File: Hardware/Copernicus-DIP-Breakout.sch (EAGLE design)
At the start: 12 parts, among them U1 COPERNICUS

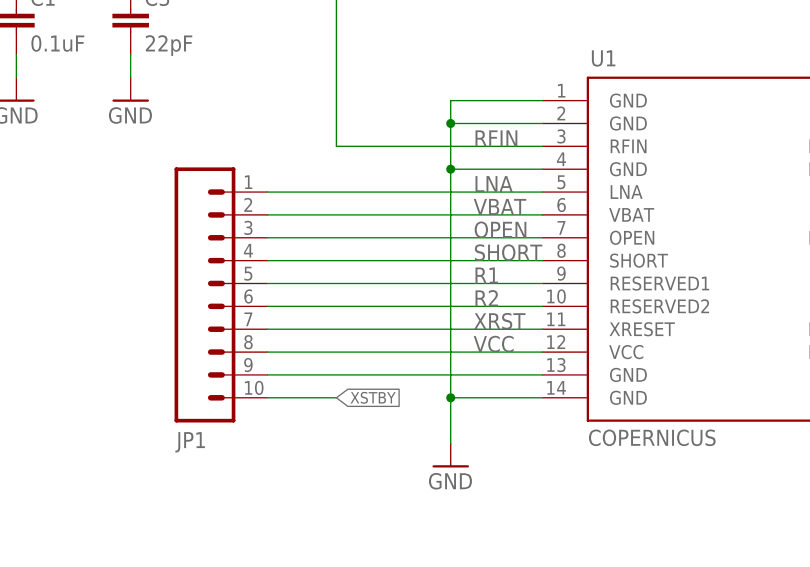
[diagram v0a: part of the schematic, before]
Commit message: Fix silk screen on board file
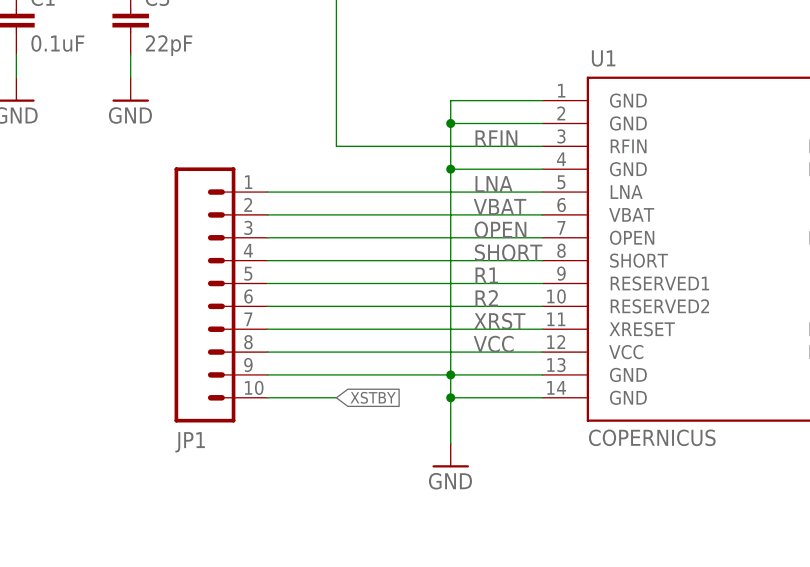
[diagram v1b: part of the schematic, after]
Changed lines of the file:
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@@
 <grid distance="0.1" unitdist="inch" unit="inch" style="lines" multiple="1" display="no" altdistance="0.01" altunitdist="inch" altunit="inch"/>
 <layers>
-<layer number="1" name="Top" color="4" fill="1" visible="yes" active="no"/>
-<layer number="2" name="Route2" color="1" fill="3" visible="yes" active="no"/>
-<layer number="3" name="Route3" color="4" fill="3" visible="yes" active="no"/>
-<layer number="4" name="Route4" color="1" fill="4" visible="yes" active="no"/>
-<layer number="5" name="Route5" color="4" fill="4" visible="yes" active="no"/>
-<layer number="6" name="Route6" color="1" fill="8" visible="yes" active="no"/>
-<layer number="7" name="Route7" color="4" fill="8" visible="yes" active="no"/>
-<layer number="8" name="Route8" color="1" fill="2" visible="yes" active="no"/>
-<layer number="9" name="Route9" color="4" fill="2" visible="yes" active="no"/>
-<layer number="10" name="Route10" color="1" fill="7" visible="yes" active="no"/>
-<layer number="11" name="Route11" color="4" fill="7" visible="yes" active="no"/>
-<layer number="12" name="Route12" color="1" fill="5" visible="yes" active="no"/>
-<layer number="13" name="Route13" color="4" fill="5" visible="yes" active="no"/>
-<layer number="14" name="Route14" color="1" fill="6" visible="yes" active="no"/>
-<layer number="15" name="Route15" color="4" fill="6" visible="yes" active="no"/>
-<layer number="16" name="Bottom" color="1" fill="1" visible="yes" active="no"/>
-<layer number="17" name="Pads" color="2" fill="1" visible="yes" active="no"/>
-<layer number="18" name="Vias" color="2" fill="1" visible="yes" active="no"/>
-<layer number="19" name="Unrouted" color="6" fill="1" visible="yes" active="no"/>
-<layer number="20" name="Dimension" color="15" fill="1" visible="yes" active="no"/>
-<layer number="21" name="tPlace" color="16" fill="1" visible="yes" active="no"/>
-<layer number="22" name="bPlace" color="14" fill="1" visible="yes" active="no"/>
-<layer number="23" name="tOrigins" color="15" fill="1" visible="yes" active="no"/>
-<layer number="24" name="bOrigins" color="15" fill="1" visible="yes" active="no"/>
-<layer number="25" name="tNames" color="7" fill="1" visible="yes" active="no"/>
-<layer number="26" name="bNames" color="7" fill="1" visible="yes" active="no"/>
-<layer number="27" name="tValues" color="7" fill="1" visible="yes" active="no"/>
-<layer number="28" name="bValues" color="7" fill="1" visible="yes" active="no"/>
+<layer number="1" name="Top" color="4" fill="1" visible="no" active="no"/>
+<layer number="2" name="Route2" color="1" fill="3" visible="no" active="no"/>
+<layer number="3" name="Route3" color="4" fill="3" visible="no" active="no"/>
+<layer number="4" name="Route4" color="1" fill="4" visible="no" active="no"/>
+<layer number="5" name="Route5" color="4" fill="4" visible="no" active="no"/>
+<layer number="6" name="Route6" color="1" fill="8" visible="no" active="no"/>
+<layer number="7" name="Route7" color="4" fill="8" visible="no" active="no"/>
+<layer number="8" name="Route8" color="1" fill="2" visible="no" active="no"/>
+<layer number="9" name="Route9" color="4" fill="2" visible="no" active="no"/>
+<layer number="10" name="Route10" color="1" fill="7" visible="no" active="no"/>
+<layer number="11" name="Route11" color="4" fill="7" visible="no" active="no"/>
+<layer number="12" name="Route12" color="1" fill="5" visible="no" active="no"/>
+<layer number="13" name="Route13" color="4" fill="5" visible="no" active="no"/>
+<layer number="14" name="Route14" color="1" fill="6" visible="no" active="no"/>
+<layer number="15" name="Route15" color="4" fill="6" visible="no" active="no"/>
+<layer number="16" name="Bottom" color="1" fill="1" visible="no" active="no"/>
+<layer number="17" name="Pads" color="2" fill="1" visible="no" active="no"/>
+<layer number="18" name="Vias" color="2" fill="1" visible="no" active="no"/>
+<layer number="19" name="Unrouted" color="6" fill="1" visible="no" active="no"/>
+<layer number="20" name="Dimension" color="15" fill="1" visible="no" active="no"/>
+<layer number="21" name="tPlace" color="16" fill="1" visible="no" active="no"/>
+<layer number="22" name="bPlace" color="14" fill="1" visible="no" active="no"/>
+<layer number="23" name="tOrigins" color="15" fill="1" visible="no" active="no"/>
+<layer number="24" name="bOrigins" color="15" fill="1" visible="no" active="no"/>
+<layer number="25" name="tNames" color="7" fill="1" visible="no" active="no"/>
+<layer number="26" name="bNames" color="7" fill="1" visible="no" active="no"/>
+<layer number="27" name="tValues" color="7" fill="1" visible="no" active="no"/>
+<layer number="28" name="bValues" color="7" fill="1" visible="no" active="no"/>
 <layer number="29" name="tStop" color="7" fill="3" visible="no" active="no"/>
 <layer number="30" name="bStop" color="7" fill="6" visible="no" active="no"/>
@@
 <layer number="35" name="tGlue" color="7" fill="4" visible="no" active="no"/>
 <layer number="36" name="bGlue" color="7" fill="5" visible="no" active="no"/>
-<layer number="37" name="tTest" color="7" fill="1" visible="yes" active="no"/>
-<layer number="38" name="bTest" color="7" fill="1" visible="yes" active="no"/>
+<layer number="37" name="tTest" color="7" fill="1" visible="no" active="no"/>
+<layer number="38" name="bTest" color="7" fill="1" visible="no" active="no"/>
 <layer number="39" name="tKeepout" color="4" fill="11" visible="no" active="no"/>
 <layer number="40" name="bKeepout" color="1" fill="11" visible="no" active="no"/>
@@
 <layer number="44" name="Drills" color="7" fill="1" visible="no" active="no"/>
 <layer number="45" name="Holes" color="7" fill="1" visible="no" active="no"/>
-<layer number="46" name="Milling" color="3" fill="1" visible="yes" active="no"/>
-<layer number="47" name="Measures" color="7" fill="1" visible="yes" active="no"/>
-<layer number="48" name="Document" color="7" fill="1" visible="yes" active="no"/>
-<layer number="49" name="Reference" color="7" fill="1" visible="yes" active="no"/>
-<layer number="50" name="dxf" color="7" fill="1" visible="yes" active="no"/>
-<layer number="51" name="tDocu" color="6" fill="1" visible="yes" active="no"/>
-<layer number="52" name="bDocu" color="7" fill="1" visible="yes" active="no"/>
-<layer number="53" name="tGND_GNDA" color="7" fill="9" visible="yes" active="no"/>
-<layer number="54" name="bGND_GNDA" color="1" fill="9" visible="yes" active="no"/>
-<layer number="56" name="wert" color="7" fill="1" visible="yes" active="no"/>
+<layer number="46" name="Milling" color="3" fill="1" visible="no" active="no"/>
+<layer number="47" name="Measures" color="7" fill="1" visible="no" active="no"/>
+<layer number="48" name="Document" color="7" fill="1" visible="no" active="no"/>
+<layer number="49" name="Reference" color="7" fill="1" visible="no" active="no"/>
+<layer number="50" name="dxf" color="7" fill="1" visible="no" active="no"/>
+<layer number="51" name="tDocu" color="6" fill="1" visible="no" active="no"/>
+<layer number="52" name="bDocu" color="7" fill="1" visible="no" active="no"/>
+<layer number="53" name="tGND_GNDA" color="7" fill="9" visible="no" active="no"/>
+<layer number="54" name="bGND_GNDA" color="1" fill="9" visible="no" active="no"/>
+<layer number="56" name="wert" color="7" fill="1" visible="no" active="no"/>
 <layer number="91" name="Nets" color="2" fill="1" visible="yes" active="yes"/>
 <layer number="92" name="Busses" color="1" fill="1" visible="yes" active="yes"/>
@@
 </segment>
 <segment>
-<wire x1="104.14" y1="81.28" x2="73.66" y2="81.28" width="0.1524" layer="91"/>
-<pinref part="U1" gate="G$2" pin="GND@4"/>
-<pinref part="JP1" gate="G$1" pin="9"/>
-</segment>
-<segment>
 <pinref part="GND2" gate="1" pin="GND"/>
 <pinref part="U1" gate="G$2" pin="GND@5"/>
@@
 <wire x1="93.98" y1="109.22" x2="93.98" y2="104.14" width="0.1524" layer="91"/>
 <junction x="93.98" y="109.22"/>
-<wire x1="93.98" y1="104.14" x2="93.98" y2="78.74" width="0.1524" layer="91"/>
+<wire x1="93.98" y1="104.14" x2="93.98" y2="81.28" width="0.1524" layer="91"/>
 <junction x="93.98" y="104.14"/>
 <junction x="93.98" y="78.74"/>
+<wire x1="93.98" y1="81.28" x2="93.98" y2="78.74" width="0.1524" layer="91"/>
+<wire x1="104.14" y1="81.28" x2="93.98" y2="81.28" width="0.1524" layer="91"/>
+<pinref part="U1" gate="G$2" pin="GND@4"/>
+<junction x="93.98" y="81.28"/>
+<pinref part="JP1" gate="G$1" pin="9"/>
+<wire x1="93.98" y1="81.28" x2="73.66" y2="81.28" width="0.1524" layer="91"/>
 </segment>
 </net>
